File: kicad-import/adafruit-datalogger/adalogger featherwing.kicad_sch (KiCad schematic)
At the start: 20 parts, among them IC1 PCF8523T, SW1 KMR2, X4 microsd, Y1 32khz

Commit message: Add initial annotation.
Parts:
- renumbered C1 to C27, C2 to C28, FID1 to FID4, FID2 to FID5, IC1 to IC3, JP3 to JP6, JP2 to JP7, JP1 to JP8, MS1 to MS2, R4 to R29, R3 to R30, R2 to R31, R1 to R32, SDCS0 to SDCS1, SJ1 to SJ5, SW1 to SW4, Y1 to Y2

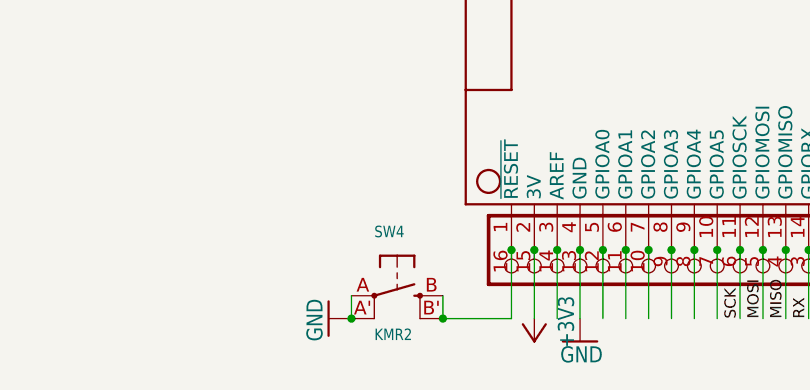
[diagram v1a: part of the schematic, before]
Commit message: Remove extra reset switches. Update notes.
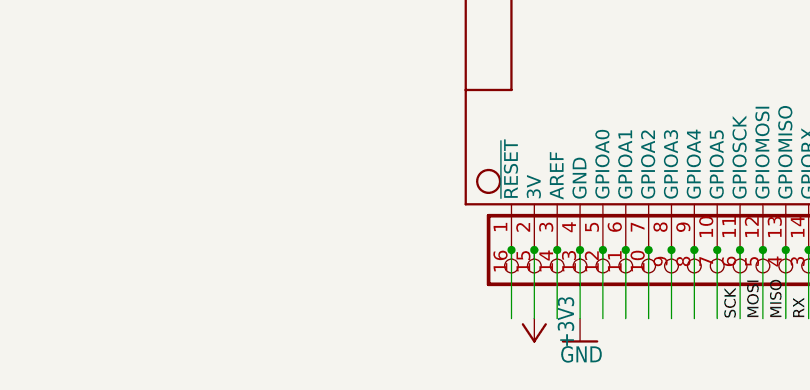
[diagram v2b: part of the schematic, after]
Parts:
- removed SW4: KMR2, adalogger featherwing:BTN_KMR2_4.6X2.8, symbol adalogger featherwing-eagle-import:SWITCH_TACT_SMT4.6X2.8
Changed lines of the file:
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@@
-	)
-	(junction
-		(at 81.28 165.1)
-		(diameter 0)
-		(color 0 0 0 0)
 	)
 	(junction
@@
 	)
 	(junction
-		(at 91.44 165.1)
-		(diameter 0)
-		(color 0 0 0 0)
-	)
-	(junction
 		(at 137.16 91.44)
 		(diameter 0)
@@
 	(wire
 		(pts
-			(xy 91.44 162.56) (xy 91.44 165.1)
-		)
-		(stroke
-			(width 0.1524)
-			(type solid)
-		)
-	)
-	(wire
-		(pts
 			(xy 193.04 99.06) (xy 180.34 99.06)
 		)
@@
 	(wire
 		(pts
-			(xy 81.28 162.56) (xy 81.28 165.1)
-		)
-		(stroke
-			(width 0.1524)
-			(type solid)
-		)
-	)
-	(wire
-		(pts
 			(xy 180.34 101.6) (xy 193.04 101.6)
 		)
@@
 		(pts
 			(xy 124.46 78.74) (xy 124.46 81.28)
-		)
-		(stroke
-			(width 0.1524)
-			(type solid)
-		)
-	)
-	(wire
-		(pts
-			(xy 91.44 165.1) (xy 99.06 165.1)
 		)
 		(stroke
@@
 	)
 	(symbol
-		(lib_id "adalogger featherwing-eagle-import:GND")
-		(at 78.74 165.1 270)
-		(mirror x)
-		(unit 1)
-		(exclude_from_sim no)
-		(in_bom yes)
-		(on_board yes)
-		(dnp no)
-		(property "Reference" "#GND05"
-			(at 78.74 165.1 0)
-			(effects
-				(font
-					(size 1.27 1.27)
-				)
-				(hide yes)
-			)
-		)
-		(property "Value" "GND"
-			(at 76.2 167.64 0)
-			(effects
-				(font
-					(size 1.778 1.5113)
-				)
-				(justify left bottom)
-			)
-		)
-		(property "Footprint" ""
-			(at 78.74 165.1 0)
-			(effects
-				(font
-					(size 1.27 1.27)
-				)
-				(hide yes)
-			)
-		)
-		(property "Datasheet" ""
-			(at 78.74 165.1 0)
-			(effects
-				(font
-					(size 1.27 1.27)
-				)
-				(hide yes)
-			)
-		)
-		(property "Description" ""
-			(at 78.74 165.1 0)
-			(effects
-				(font
-					(size 1.27 1.27)
-				)
-				(hide yes)
-			)
-		)
-		(pin "1"
-		)
-		(instances
-			(project ""
-				(path "/513b855f-afaa-458f-b216-457a372f9dfa"
-					(reference "#GND2")
-					(unit 1)
-				)
-			)
-			(project "Genesis"
-				(path "/66b8af00-4ede-44e3-a762-88857219665d/9d55f160-1827-4393-a821-340d91310655"
-					(reference "#GND05")
-					(unit 1)
-				)
-			)
-		)
-	)
-	(symbol
 		(lib_id "adalogger featherwing-eagle-import:+3V3")
 		(at 101.6 167.64 180)
@@
 					(unit 1)
 				)
-			)
-		)
-	)
-	(symbol
-		(lib_id "adalogger featherwing-eagle-import:SWITCH_TACT_SMT4.6X2.8")
-		(at 86.36 162.56 0)
-		(unit 1)
-		(exclude_from_sim no)
-		(in_bom yes)
-		(on_board yes)
-		(dnp no)
-		(property "Reference" "SW4"
-			(at 83.82 156.21 0)
-			(effects
-				(font
-					(size 1.27 1.0795)
-				)
-				(justify left bottom)
-			)
-		)
-		(property "Value" "KMR2"
-			(at 83.82 167.64 0)
-			(effects
-				(font
-					(size 1.27 1.0795)
-				)
-				(justify left bottom)
-			)
-		)
-		(property "Footprint" "adalogger featherwing:BTN_KMR2_4.6X2.8"
-			(at 86.36 162.56 0)
-			(effects
-				(font
-					(size 1.27 1.27)
-				)
-				(hide yes)
-			)
-		)
-		(property "Datasheet" ""
-			(at 86.36 162.56 0)
-			(effects
-				(font
-					(size 1.27 1.27)
-				)
-				(hide yes)
-			)
-		)
-		(property "Description" ""
-			(at 86.36 162.56 0)
-			(effects
-				(font
-					(size 1.27 1.27)
-				)
-				(hide yes)
-			)
-		)
-		(pin "A"
-		)
-		(pin "A'"
-		)
-		(pin "B"
-		)
-		(pin "B'"
-		)
-		(instances
-			(project ""
-				(path "/513b855f-afaa-458f-b216-457a372f9dfa"
-					(reference "SW1")
-					(unit 1)
-				)
-			)
-			(project "Genesis"
-				(path "/66b8af00-4ede-44e3-a762-88857219665d/9d55f160-1827-4393-a821-340d91310655"
-					(reference "SW4")
-					(unit 1)
-				)

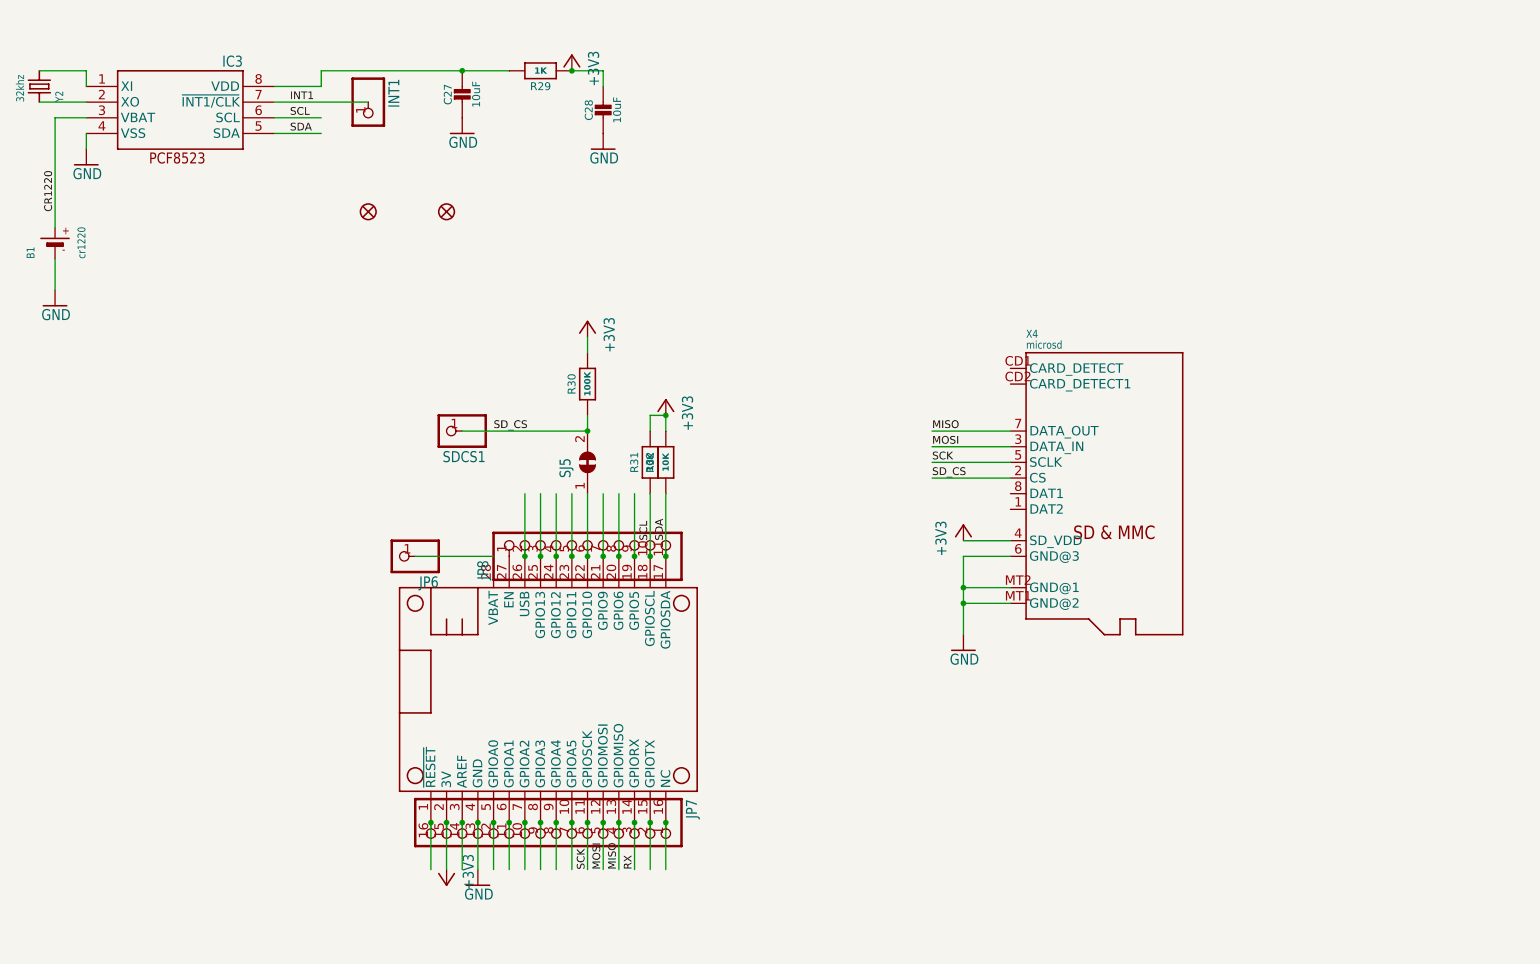
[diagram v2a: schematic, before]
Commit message: Change power net on RTC page to match global. Change buffered MISO net name on ETH PHY to allow global MISO.
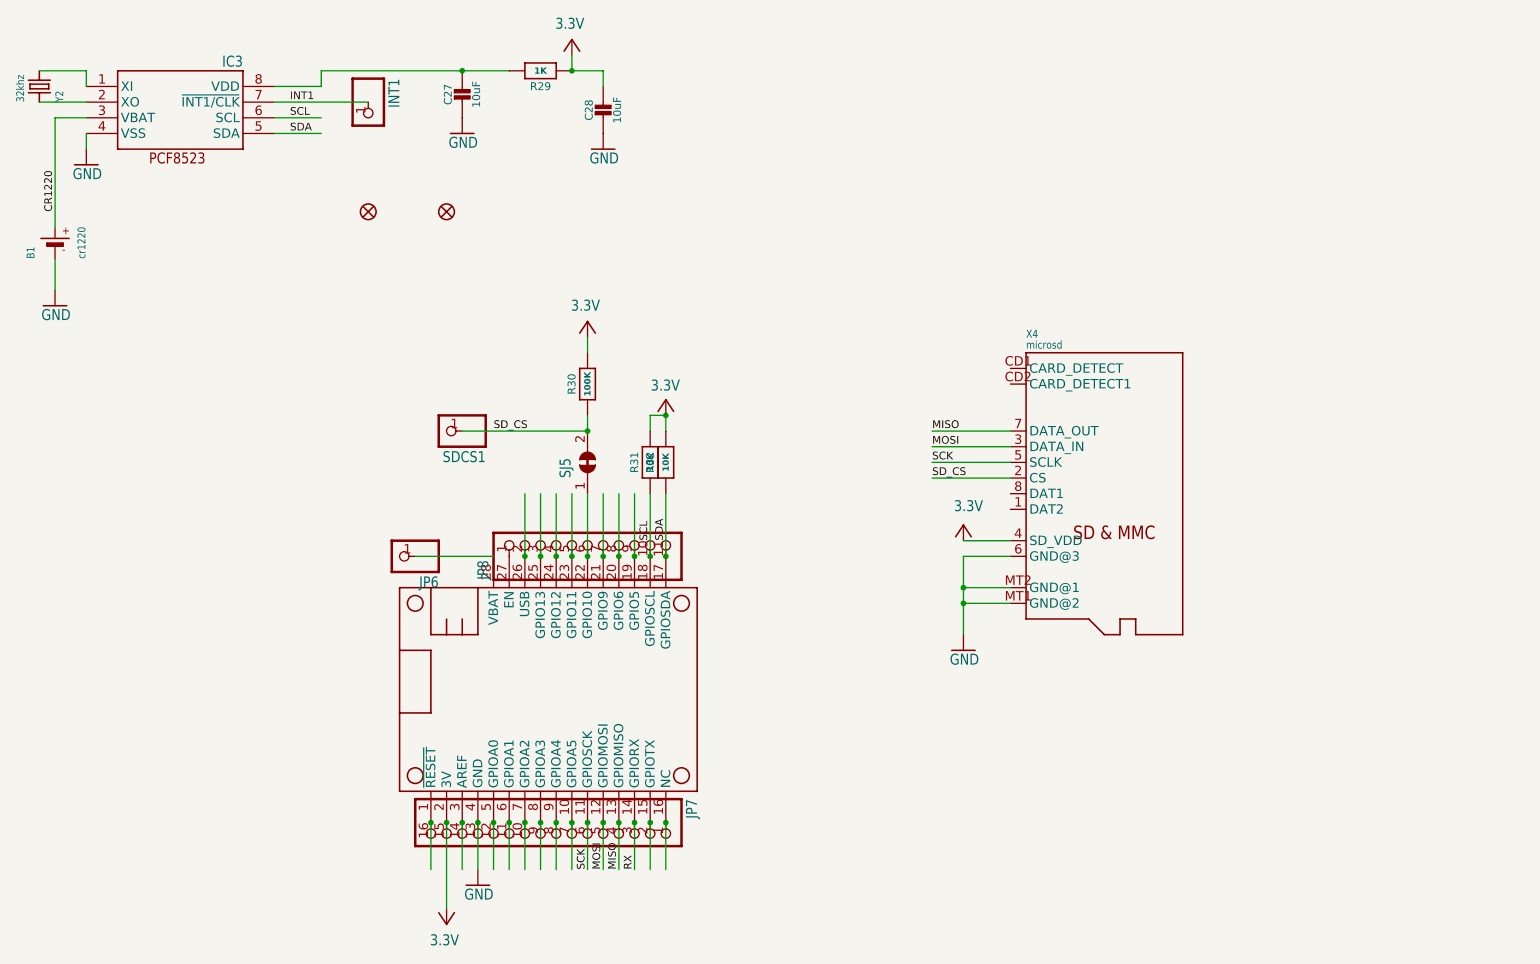
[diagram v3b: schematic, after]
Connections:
- net +3V3 renamed 3.3V
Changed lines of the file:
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@@
+	(wire
+		(pts
+			(xy 121.92 33.02) (xy 121.92 35.56)
+		)
+		(stroke
+			(width 0)
+			(type default)
+		)
+	)
 	(wire
 		(pts
@@
 	(wire
 		(pts
-			(xy 101.6 165.1) (xy 101.6 157.48)
+			(xy 101.6 171.45) (xy 101.6 157.48)
 		)
 		(stroke
@@
 	(symbol
 		(lib_id "adalogger featherwing-eagle-import:+3V3")
-		(at 101.6 167.64 180)
+		(at 101.6 173.99 180)
 		(unit 1)
 		(exclude_from_sim no)
@@
 		(dnp no)
 		(property "Reference" "#+3V01"
-			(at 101.6 167.64 0)
-			(effects
-				(font
-					(size 1.27 1.27)
-				)
-				(hide yes)
-			)
-		)
-		(property "Value" "+3V3"
-			(at 104.14 162.56 90)
+			(at 101.6 173.99 0)
+			(effects
+				(font
+					(size 1.27 1.27)
+				)
+				(hide yes)
+			)
+		)
+		(property "Value" "3.3V"
+			(at 103.632 175.514 0)
 			(effects
 				(font
@@
 		)
 		(property "Footprint" ""
-			(at 101.6 167.64 0)
-			(effects
-				(font
-					(size 1.27 1.27)
-				)
-				(hide yes)
-			)
-		)
-		(property "Datasheet" ""
-			(at 101.6 167.64 0)
-			(effects
-				(font
-					(size 1.27 1.27)
-				)
-				(hide yes)
-			)
-		)
-		(property "Description" ""
-			(at 101.6 167.64 0)
+			(at 101.6 173.99 0)
+			(effects
+				(font
+					(size 1.27 1.27)
+				)
+				(hide yes)
+			)
+		)
+		(property "Datasheet" ""
+			(at 101.6 173.99 0)
+			(effects
+				(font
+					(size 1.27 1.27)
+				)
+				(hide yes)
+			)
+		)
+		(property "Description" ""
+			(at 101.6 173.99 0)
 			(effects
 				(font
@@
 			)
 		)
-		(property "Value" "+3V3"
-			(at 182.88 114.3 90)
+		(property "Value" "3.3V"
+			(at 183.896 107.188 0)
 			(effects
 				(font
@@
 	(symbol
 		(lib_id "adalogger featherwing-eagle-import:+3V3")
-		(at 121.92 33.02 0)
+		(at 121.92 30.48 0)
 		(mirror y)
 		(unit 1)
@@
 		(dnp no)
 		(property "Reference" "#+3V02"
-			(at 121.92 33.02 0)
-			(effects
-				(font
-					(size 1.27 1.27)
-				)
-				(hide yes)
-			)
-		)
-		(property "Value" "+3V3"
-			(at 124.46 38.1 90)
+			(at 121.92 30.48 0)
+			(effects
+				(font
+					(size 1.27 1.27)
+				)
+				(hide yes)
+			)
+		)
+		(property "Value" "3.3V"
+			(at 123.952 28.956 0)
 			(effects
 				(font
@@
 		)
 		(property "Footprint" ""
-			(at 121.92 33.02 0)
-			(effects
-				(font
-					(size 1.27 1.27)
-				)
-				(hide yes)
-			)
-		)
-		(property "Datasheet" ""
-			(at 121.92 33.02 0)
-			(effects
-				(font
-					(size 1.27 1.27)
-				)
-				(hide yes)
-			)
-		)
-		(property "Description" ""
-			(at 121.92 33.02 0)
+			(at 121.92 30.48 0)
+			(effects
+				(font
+					(size 1.27 1.27)
+				)
+				(hide yes)
+			)
+		)
+		(property "Datasheet" ""
+			(at 121.92 30.48 0)
+			(effects
+				(font
+					(size 1.27 1.27)
+				)
+				(hide yes)
+			)
+		)
+		(property "Description" ""
+			(at 121.92 30.48 0)
 			(effects
 				(font
@@
 			)
 		)
-		(property "Value" "+3V3"
-			(at 127 81.28 90)
+		(property "Value" "3.3V"
+			(at 126.492 74.676 0)
 			(effects
 				(font
@@
 			)
 		)
-		(property "Value" "+3V3"
-			(at 139.7 93.98 90)
-			(effects
-				(font
+		(property "Value" "3.3V"
+			(at 139.446 87.63 0)
+			(effects
+				(font
